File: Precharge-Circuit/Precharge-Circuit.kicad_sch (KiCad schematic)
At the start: 37 parts, among them J1 Conn_01x05, J2 19427-0040, J3 XH_2pin_Side, J4 XH_2pin_Side, K1 AZDC6-2AE-12D, K2 G5Q-1A4_DC12, K3 G5Q-1A4_DC12, Q1 2N7002K-AU, Q2 2N7002K-AU, Q3 2N7002K-AU, Q4 2N7002K-AU

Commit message: 用紙サイズ変更
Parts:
- added U1, U2: TLP291(GB,SE, ProjectEV:Isolator_TLP291(GB,SE, symbol ProjectEV:Isolator_TLP291(GB,SE
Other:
- note added: "<- from Precharge Registor -> to TS+"
- moved on the sheet: C1, C2, C3, C4, D1, D10, D11, D2, D3, D4, D5, D6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

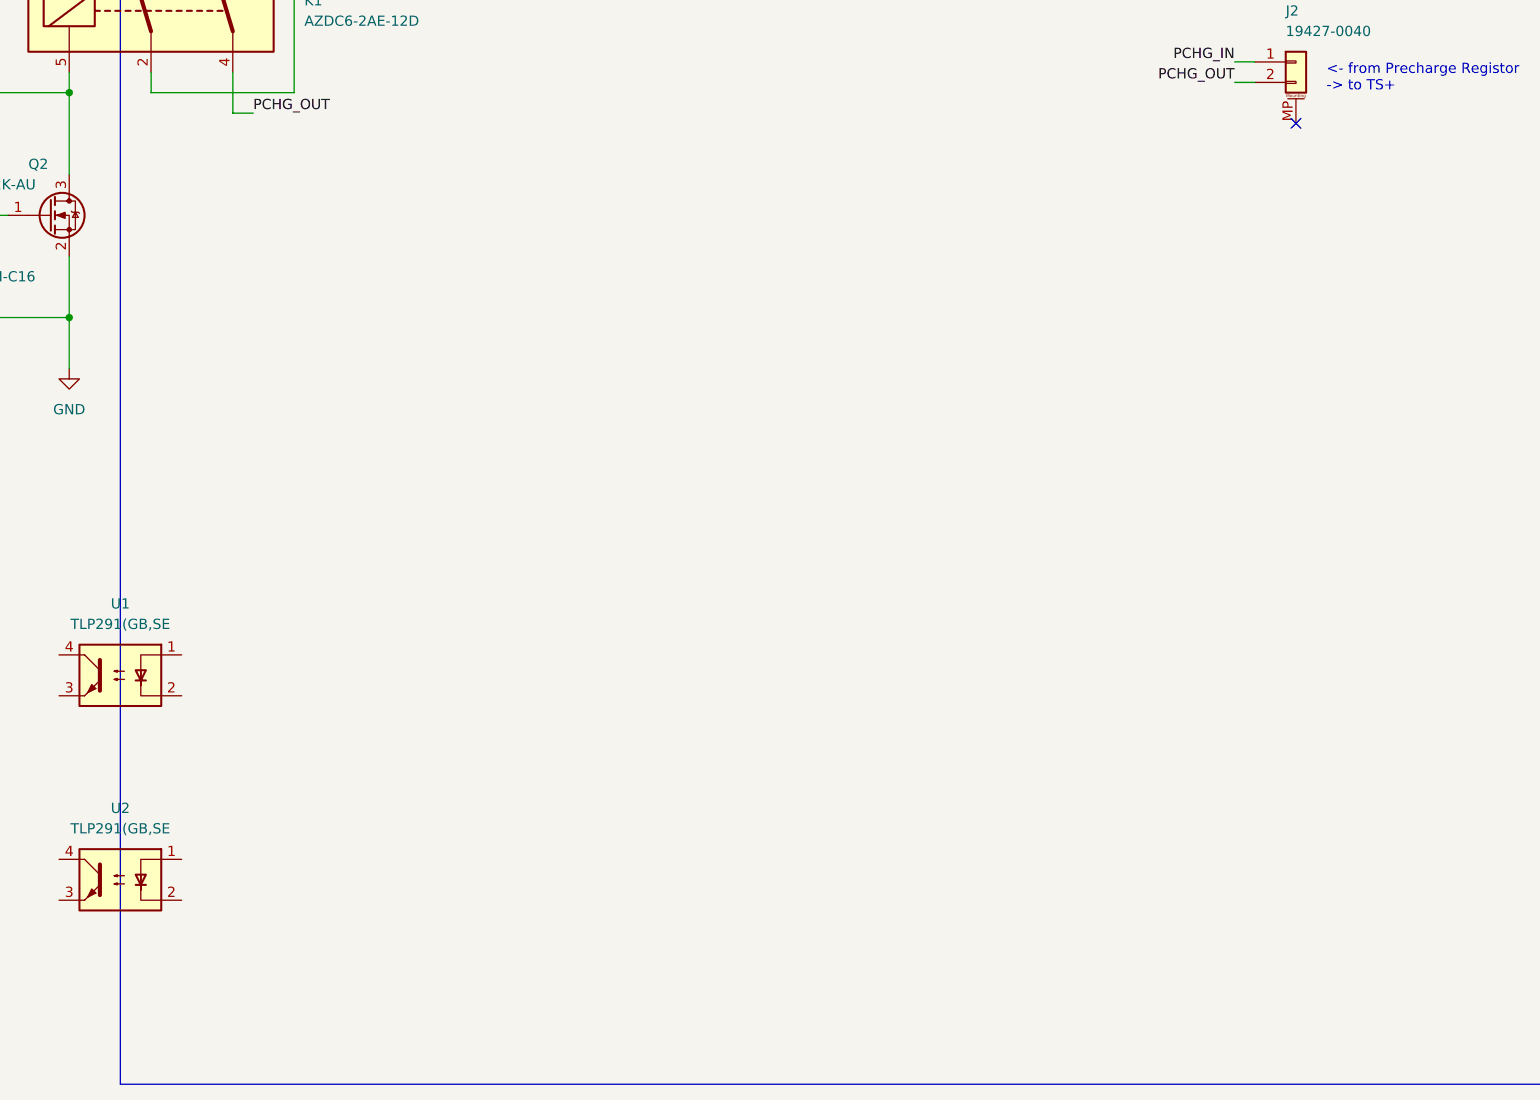
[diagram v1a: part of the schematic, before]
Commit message: 電圧検知追加
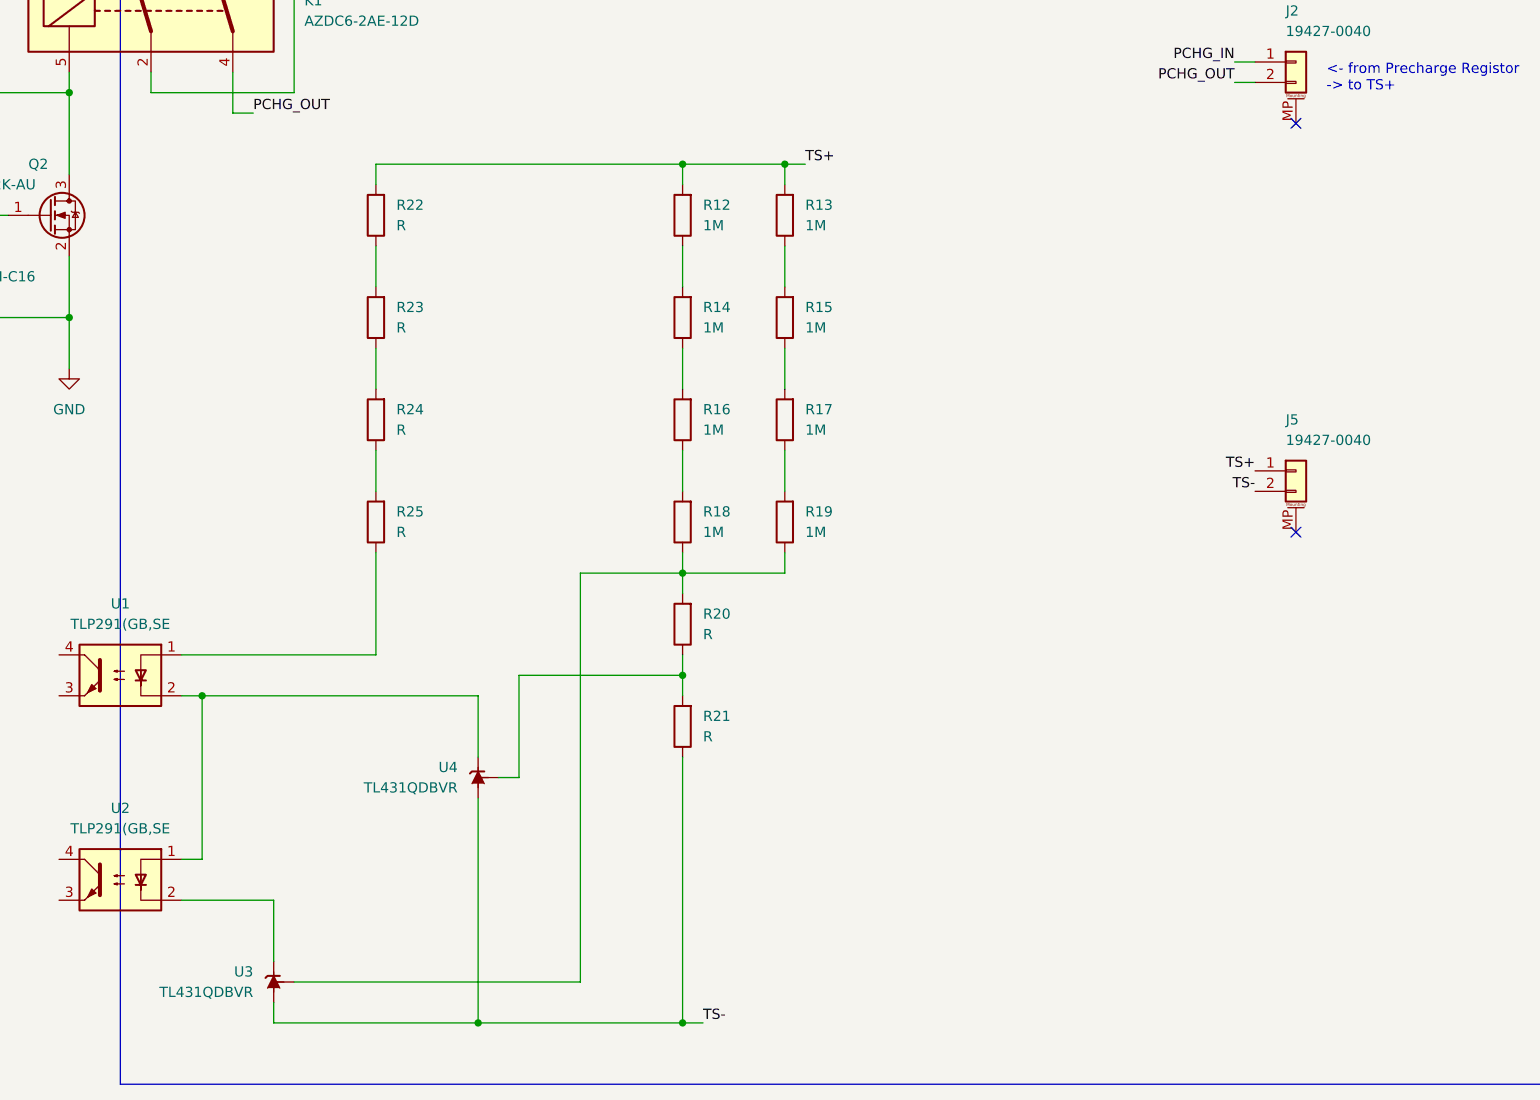
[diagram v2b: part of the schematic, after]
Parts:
- added J5: 19427-0040, ProjectEV:Connector_MX150L_19427-0040, symbol ProjectEV:Connector_MX150L_19427-0040
- added R12, R13, R14, R15, R16, R17, R18, R19: 1M, Resistor_SMD:R_1206_3216Metric, symbol Device:R
- added R20, R21, R22, R23, R24, R25: R, symbol Device:R
- added U3, U4: TL431QDBVR, ProjectEV:Package_SOT-23-5_TL431QDBVR, symbol ProjectEV:Reference_TL431QDBVR
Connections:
- net at U2.1 (Anode): now also U1.2 (Cathode), U4.3 (K)
- net at U2.2 (Cathode): now also U3.3 (K)
- net at U1.1 (Anode): now also R25.1
- new net: R14.1, R16.2
- new net: R12.1, R14.2
- new net: R23.1, R24.2
- new net: R22.1, R23.2
- new net: R24.1, R25.2
- new net: R18.1, R19.1, R20.2, U3.4 (REF)
- new net: R16.1, R18.2
- new net: R15.1, R17.2
- new net: R13.1, R15.2
- new net: R20.1, R21.2, U4.4 (REF)
- new net: R17.1, R19.2
- new net TS+: J5.1 (Pin_1), R12.2, R13.2, R22.2
- new net TS-: J5.2 (Pin_2), R21.1, U3.5 (A), U3.6 (A), U3.7 (A), U4.5 (A), U4.6 (A), U4.7 (A)
- no-connect marks 1 -> 2

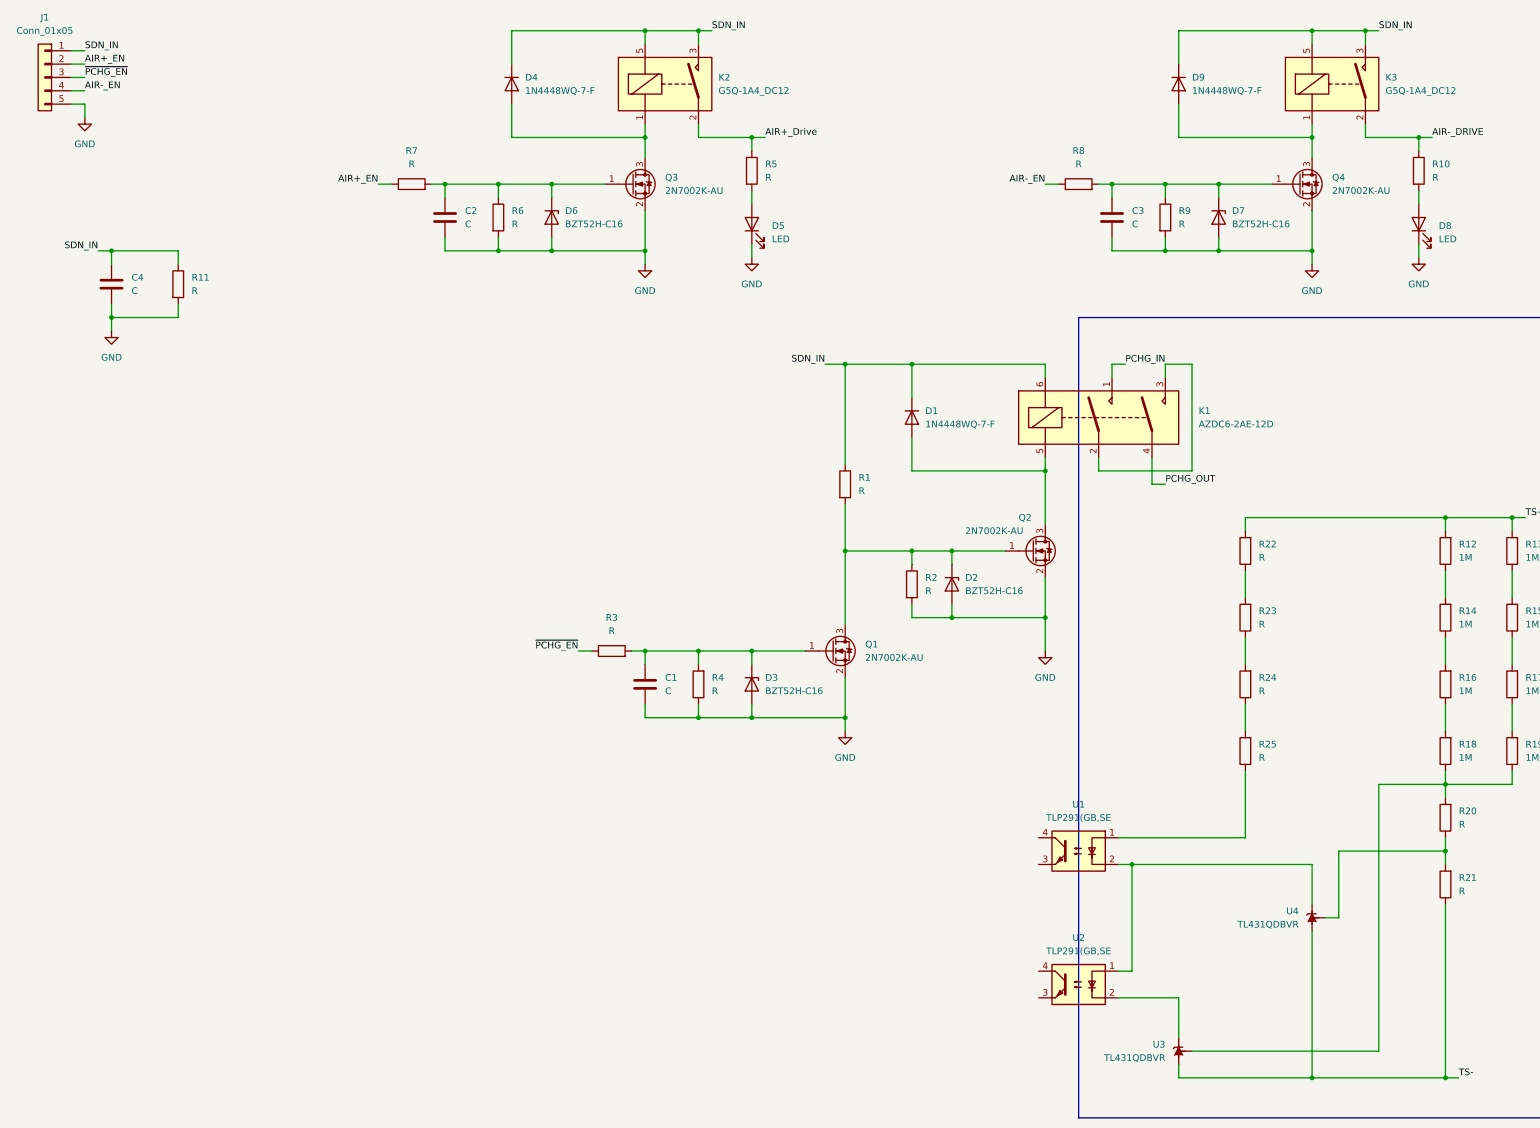
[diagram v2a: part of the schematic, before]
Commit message: 12V電源入力追加
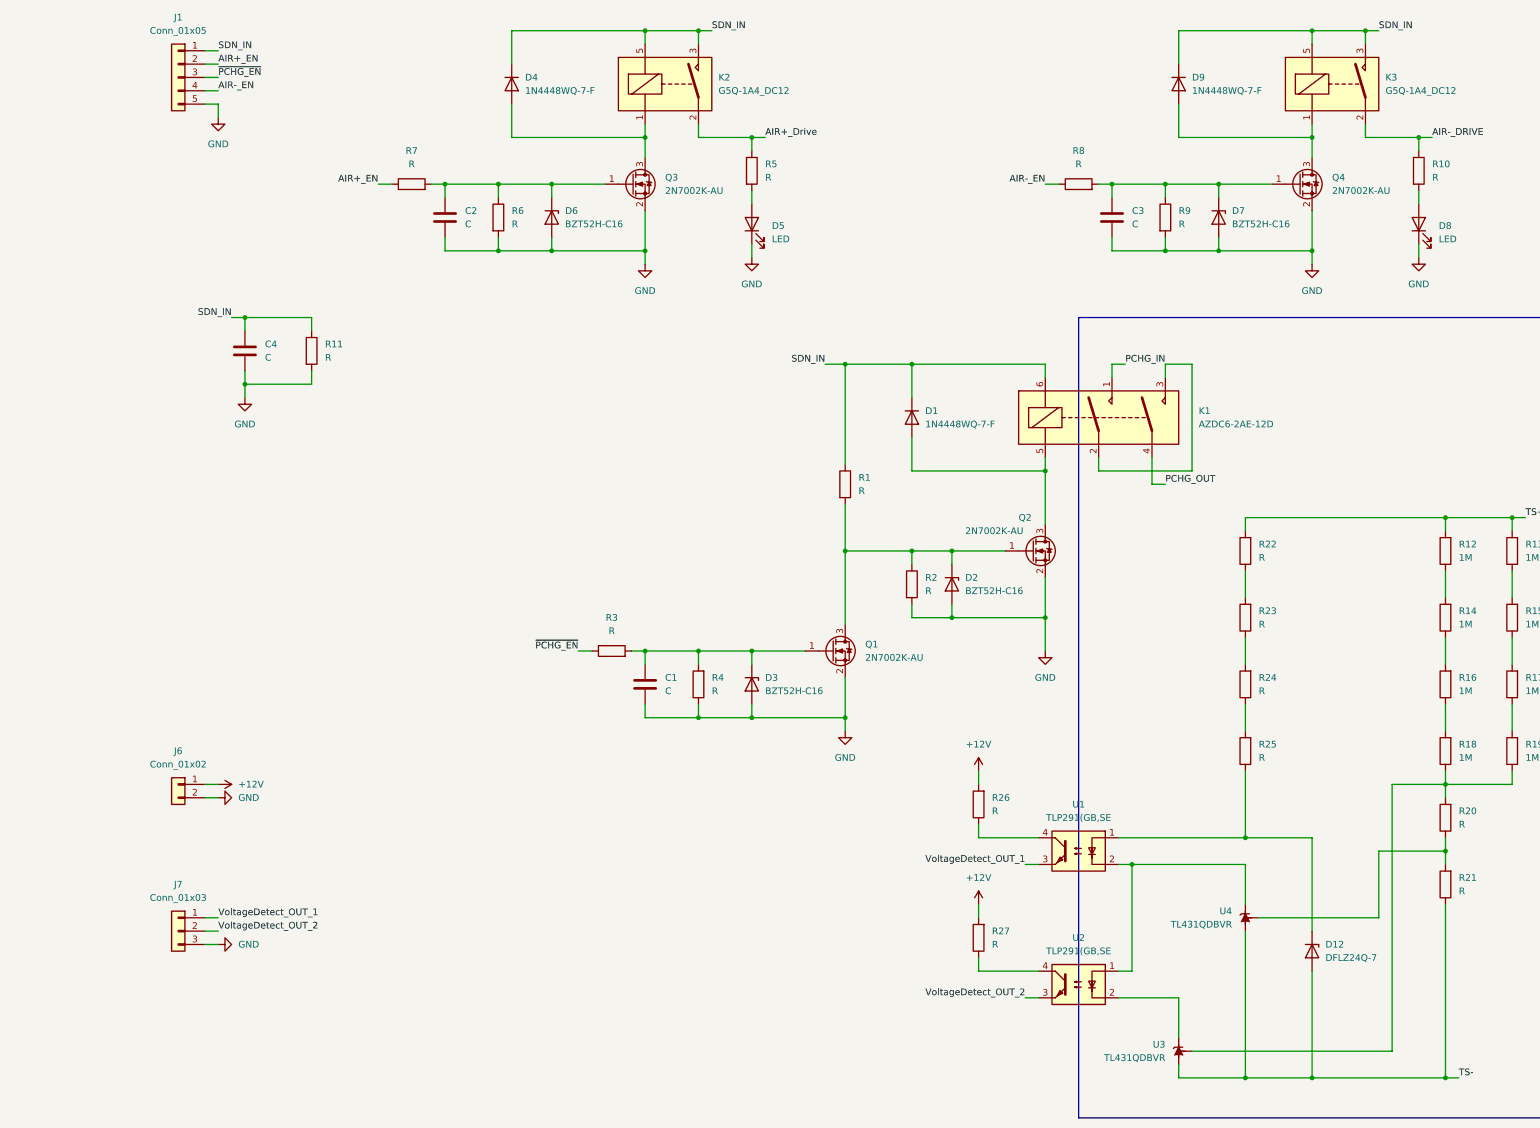
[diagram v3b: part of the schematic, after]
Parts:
- added D12: DFLZ24Q-7, ProjectEV:D_PowerDI-123_DFLZxxQ, symbol ProjectEV:D_DFLZ24Q-7
- added J6: Conn_01x02, symbol Connector_Generic:Conn_01x02
- added J7: Conn_01x03, symbol Connector_Generic:Conn_01x03
- added R26, R27: R, symbol Device:R
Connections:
- net GND: now also J6.2 (Pin_2), J7.3 (Pin_3)
- net TS-: now also D12.2 (A)
- net VoltageDetect_OUT_2: now reaches U2.3 (Emitter)
- net VoltageDetect_OUT_2: now also J7.2 (Pin_2)
- net at U2.4 (Collector): now also R27.1
- net at R25.1, U1.1 (Anode): now also D12.1 (K)
- net VoltageDetect_OUT_1: now reaches U1.3 (Emitter)
- net VoltageDetect_OUT_1: now also J7.1 (Pin_1)
- net at U1.4 (Collector): now also R26.1
- new net +12V: J6.1 (Pin_1), R26.2, R27.2
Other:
- moved on the sheet: C4, J1, R11, U4

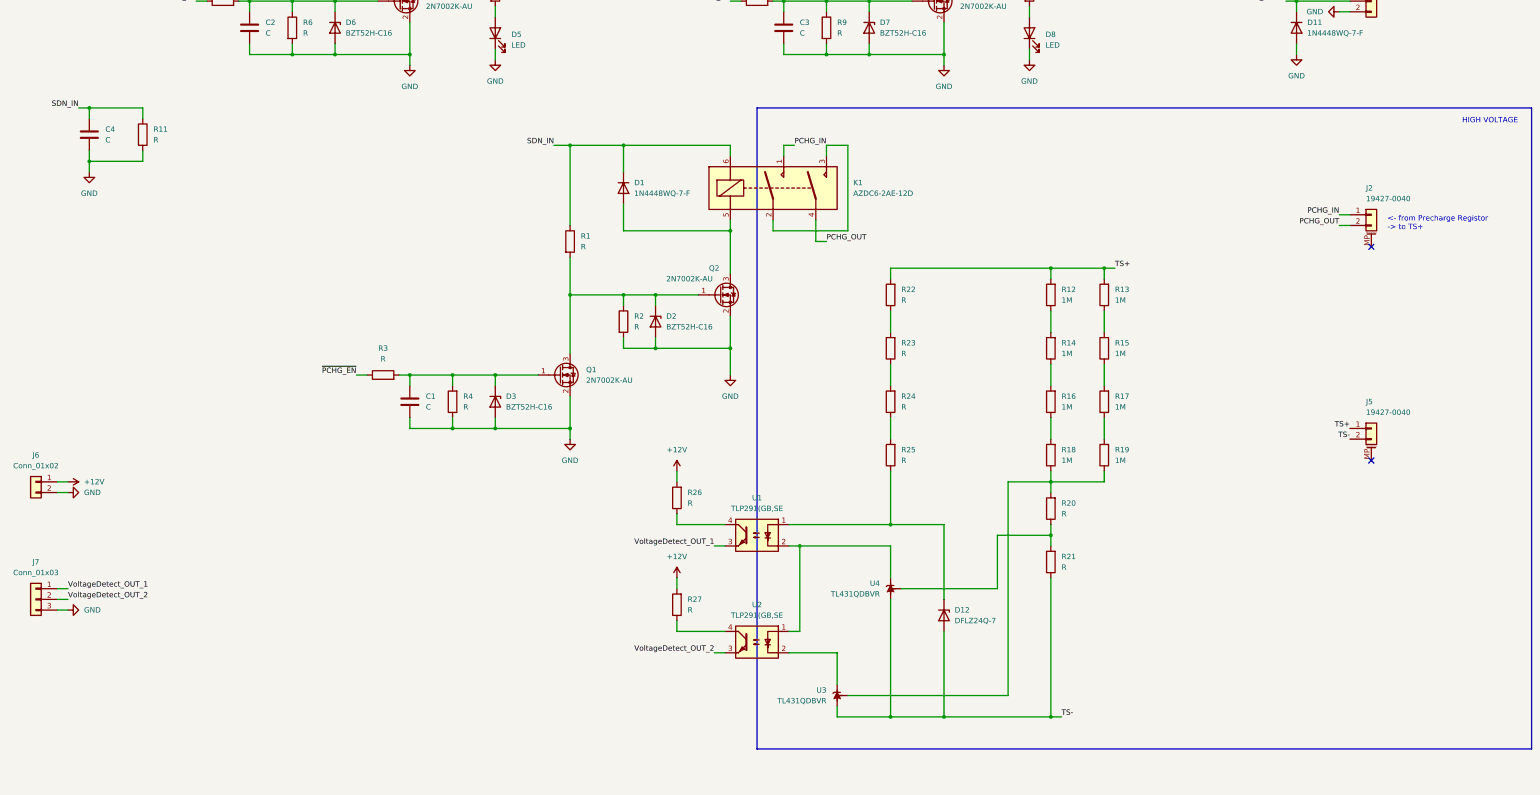
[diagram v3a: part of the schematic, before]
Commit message: 電圧検知信号ライン修正
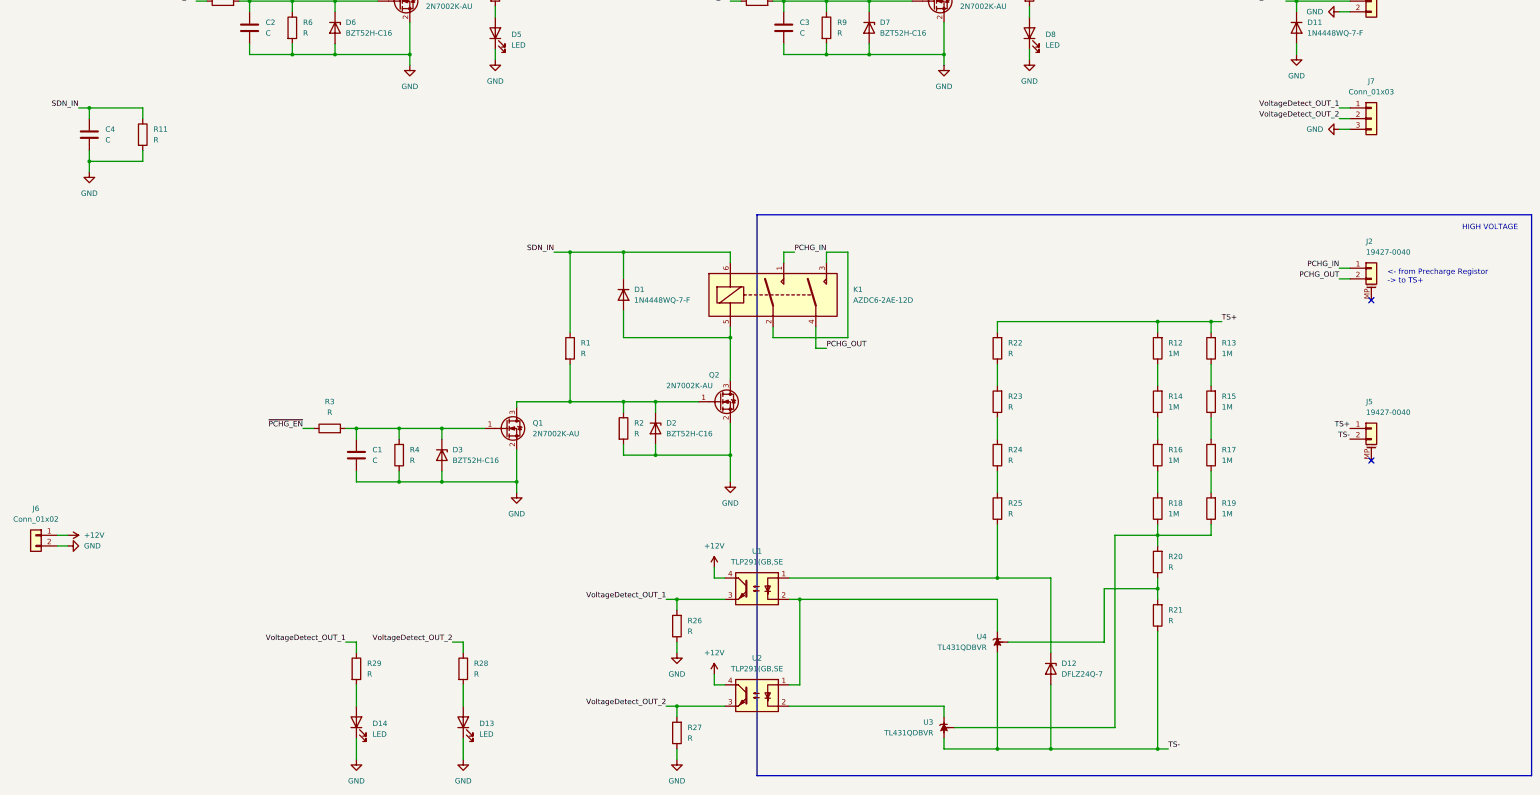
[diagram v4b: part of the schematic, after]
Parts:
- added D13, D14: LED, symbol Device:LED
- added R28, R29: R, symbol Device:R
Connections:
- net +12V: now also U1.4 (Collector), U2.4 (Collector); no longer R26.2, R27.2
- net GND: now also R26.1, R27.1, D13.1 (K), D14.1 (K)
- net VoltageDetect_OUT_1: now also R26.2, R29.1
- net VoltageDetect_OUT_2: now also R27.2, R28.1
- new net: D14.2 (A), R29.2
- new net: D13.2 (A), R28.2
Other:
- moved on the sheet: C1, D1, D12, D2, D3, J2, J6, J7, K1, Q1, Q2, R1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
